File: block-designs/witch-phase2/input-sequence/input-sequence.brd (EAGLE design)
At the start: 98.8 x 75.2 mm, 61 parts, among them IC1 74AHC1G08DBV, IC10 741G175, IC11 741G175, IC12 741G175, IC13 74AHC1G32DBV, IC14 74AHC1G32DBV, IC15 74AHC1G32DBV, IC16 74AHC1G32DBV, IC17 74AHC1G32DBV, IC18 74AHC1G32DBV, IC19 4017D, IC2 74AHC1G08DBV, IC20 74LVC1G14DBV, IC21 74LVC1G14DBV, IC22 74AHC1G08DBV, IC23 74LVC1G14DBV, IC3 74AHC1G08DBV, IC4 74AHC1G08DBV, IC5 74AHC1G08DBV, IC6 74AHC1G08DBV, IC7 741G175, IC8 741G175, IC9 741G175

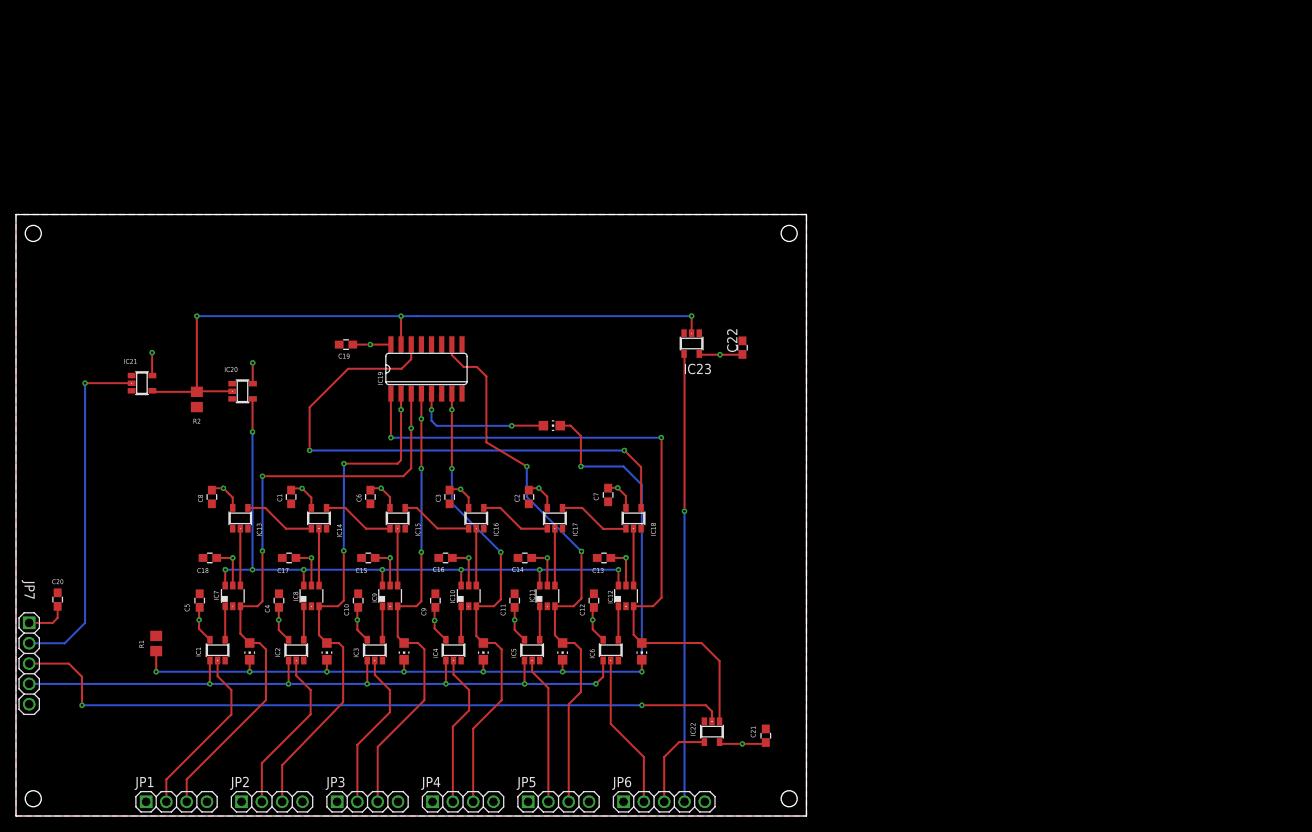
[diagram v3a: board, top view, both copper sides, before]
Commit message: rework design: reduced logic to minimum, added 555 timer for debouncing moved encoder connector to top edge of board for easy routing of cabling, changed the pulse-generator connector back to 4-pin for easy cabling, cleaned up all the core routing and run detailed drc
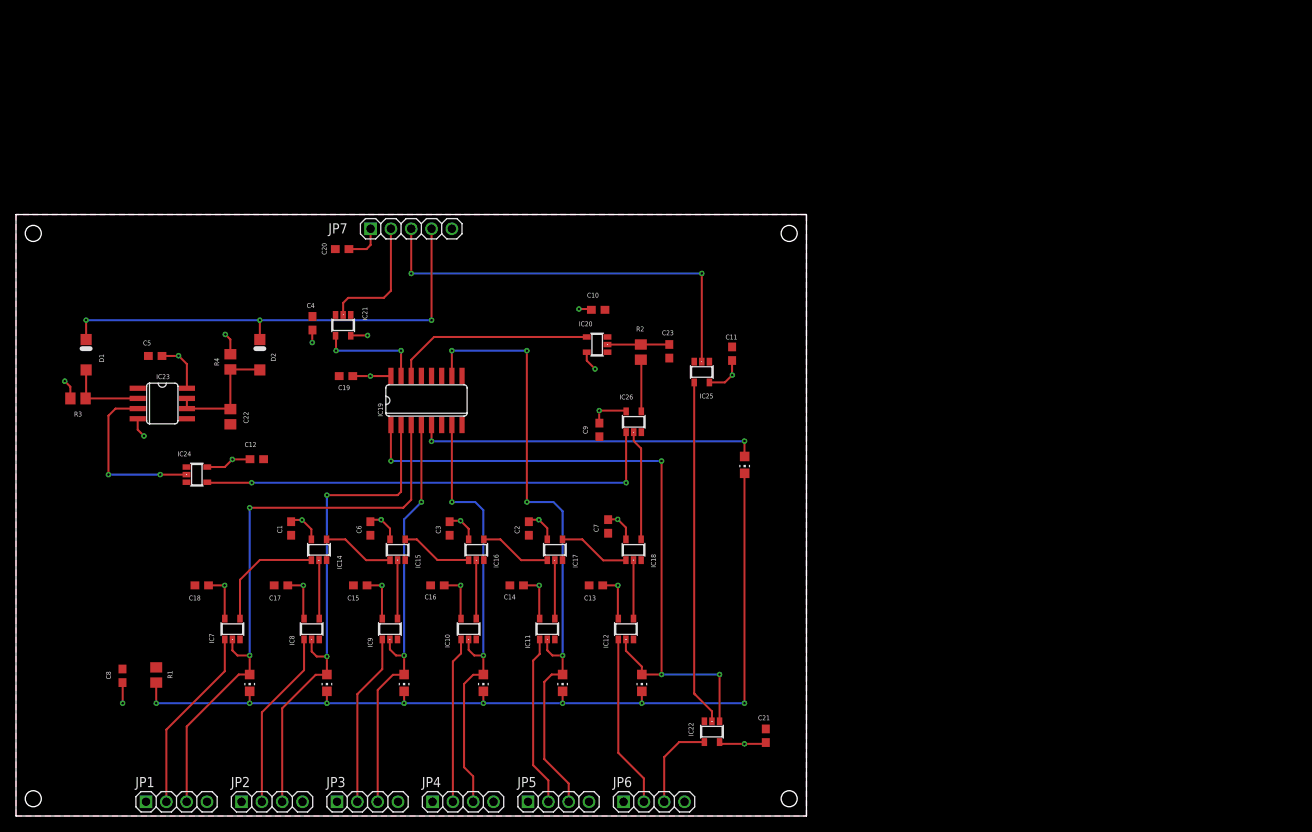
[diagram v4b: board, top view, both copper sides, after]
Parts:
- removed IC1, IC2, IC3, IC4, IC5, IC6: 74AHC1G08DBV, 74xx-little-us:SOT23-5
- removed IC13: 74AHC1G32DBV, 74xx-little-us:SOT23-5
- added C23: 0.1uF, resistor:C0603
- added D1, D2: MBR0520LT, diode:SOD123
- added IC24: 74LVC1G14DBV, 74xx-little-us:SOT23-5
- added IC25: 74LVC1G17DBV, 74xx-little-us:SOT23-5
- added IC26: 74AHC1G08DBV, 74xx-little-us:SOT23-5
- added R3: 100K, resistor:R0805
- added R4: 47K, resistor:R0805
- C22: value 0.1uF -> 10uF; device resistor:C0603 -> resistor:C0805
- IC10, IC11, IC12, IC7, IC8, IC9: value 741G175 -> 74AHC1G08DBV; device witch-e:DBV_R-PDSO-G6 -> 74xx-little-us:SOT23-5
- IC20: value 74LVC1G14DBV -> 74LVC1G17DBV
- IC23: value 74LVC1G14DBV -> NE555D; device 74xx-little-us:SOT23-5 -> adafruit:SO08
- JP6: device custom-pinhead:1X05 -> custom-pinhead:1X04
- R1: value (none) -> 270R
- R2: value (none) -> 1K
- moved JP7 72.4 mm to (49.4, 73.4), turned to 0 degrees
- moved IC23 66.6 mm to (18.3, 51.6), turned to 270 degrees
- moved C22 64.6 mm to (26.8, 49.9), turned to 270 degrees
- moved C20 56.4 mm to (40.8, 70.9), turned to 180 degrees
- moved R2 55.8 mm to (78.1, 58.0), turned to 270 degrees
- moved C10 47.1 mm to (72.8, 63.3), turned to 0 degrees
- moved C12 45.7 mm to (30.1, 44.6), turned to 0 degrees
- moved IC20 44.7 mm to (72.6, 58.9), turned to 90 degrees
- moved C11 41.1 mm to (89.5, 57.8)
- moved C4 34.9 mm to (37.1, 61.6)
- moved C5 31.1 mm to (17.4, 57.5), turned to 180 degrees
- moved C9 29.6 mm to (72.9, 48.3), turned to 270 degrees
- moved IC21 26.2 mm to (40.9, 61.3), turned to 180 degrees
- moved C8 25.0 mm to (13.3, 17.5), turned to 90 degrees
- moved LED7 24.6 mm to (91.1, 43.9), turned to 180 degrees
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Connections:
- net NEXT2 renamed CLK1
- net NEXT3 renamed CLK2
- net NEXT4 renamed CLK3
- net NEXT5 renamed CLK4
- removed net !RESET: IC10.6, IC11.6, IC12.6, IC20.4, IC7.6, IC8.6, IC9.6
- removed net !RST_OUT: IC23.4, JP6.4
- removed net N$1: IC2.4, IC8.1
- removed net N$2: IC1.4, IC7.1
- removed net N$3: IC3.4, IC9.1
- removed net N$4: IC10.1, IC4.4
- removed net N$5: IC11.1, IC5.4
- removed net N$6: IC12.1, IC6.4
- removed net NEXT1: IC13.4, IC14.1
- removed net NEXT6: IC18.4, IC19.14
- new net !KEY_IN: D1.C, D2.C, JP7.4
- new net CLK5: IC18.4, IC26.2
- new net N$10: D1.A, IC23.2, R3.1
- new net N$11: IC23.3, IC24.2
- new net N$12: IC25.2, JP7.3
- new net N$13: C23.1, IC20.2, R2.1
- new net N$14: IC26.4, R2.2
- new net N$8: IC19.14, IC20.4
- new net N$9: C22.1, D2.A, IC23.6, IC23.7, R4.1
- net !KEY: now also IC24.4, IC26.1; no longer IC1.1, IC2.1, IC3.1, IC4.1, IC5.1, IC6.1, JP7.4
- net EXEC: now also IC25.4; no longer JP7.3
- net GND: now also C23.2, IC10.3, IC11.3, IC12.3, IC23.1, IC24.3, IC25.3, IC26.3, IC7.3, IC8.3, IC9.3, JP6.4; no longer IC1.3, IC10.2, IC11.2, IC12.2, IC13.1, IC13.3, IC2.3, IC23.3, IC3.3, IC4.3, IC5.3, IC6.3, IC7.2, IC8.2, IC9.2, JP6.5, R2.1
- net RESET: no longer IC20.2, IC23.2, R2.2
- net SEL1: now also IC7.2; no longer IC7.3
- net SEL2: now also IC8.2; no longer IC8.3
- net SEL3: now also IC9.2; no longer IC9.3
- net SEL4: now also IC10.2; no longer IC10.3
- net SEL5: now also IC11.2; no longer IC11.3
- net SEL6: now also IC12.2; no longer IC12.3
- net STEP1: now also IC14.1; no longer IC13.2
- net VAL1: now also IC7.1; no longer IC1.2
- net VAL2: now also IC8.1; no longer IC2.2
- net VAL3: now also IC9.1; no longer IC3.2
- net VAL4: now also IC10.1; no longer IC4.2
- net VAL5: now also IC11.1; no longer IC5.2
- net VAL6: now also IC12.1; no longer IC6.2
- net VCC: now also IC23.4, IC23.8, IC24.5, IC25.5, IC26.5, R3.2, R4.2; no longer C22.1, IC1.5, IC13.5, IC2.5, IC23.5, IC3.5, IC4.5, IC5.5, IC6.5
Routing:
- net !RESET: track 82.4 -> 0.00 mm, vias 8 -> 0
- net RESET: track 87.0 -> 13.4 mm, vias 3 -> 2
- net NEXT6: track 69.8 -> 0.00 mm, vias 2 -> 0
- net !KEY_IN: track 0.00 -> 59.4 mm, vias 0 -> 3
- net !RST_OUT: track 56.0 -> 0.00 mm, vias 1 -> 0
- net N$12: track 0.00 -> 52.9 mm, vias 0 -> 2
- net EXEC: track 91.1 -> 43.3 mm, vias 2 -> 0
- net !KEY: track 88.8 -> 58.7 mm, vias 6 -> 2
- net !CLEAR: track 43.8 -> 15.9 mm, vias 1 -> 0
- net SEL7: track 17.7 -> 43.2 mm
- net N$8: track 0.00 -> 25.1 mm
- net N$11: track 0.00 -> 21.2 mm, vias 0 -> 2
- net N$9: track 0.00 -> 15.4 mm
- net CLK5: track 0.00 -> 13.8 mm
- net N$10: track 0.00 -> 10.1 mm
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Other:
- board text added: "Revison 3"
